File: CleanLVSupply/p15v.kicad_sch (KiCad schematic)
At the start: 19 parts, among them U3 LMR64010XMF, U4 TPS7A47

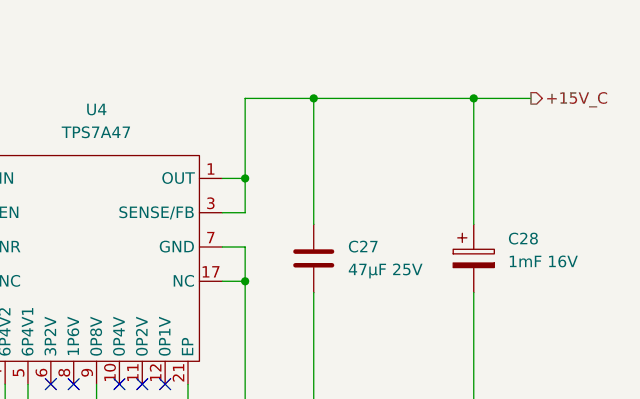
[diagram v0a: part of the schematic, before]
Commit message: HiFiDAC routing done, CleanLVSupply fuses added
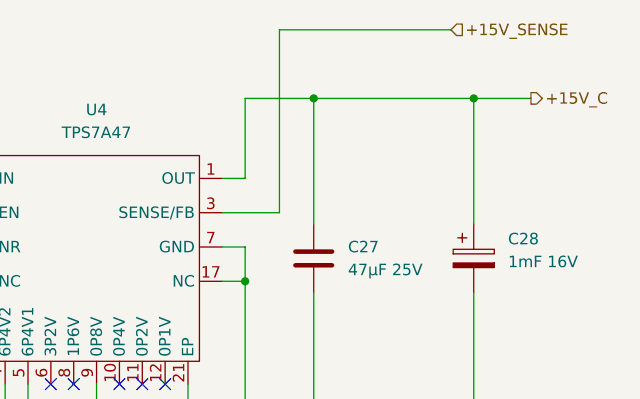
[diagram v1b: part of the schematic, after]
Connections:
- net +15V_C: no longer U4.3 (SENSE/FB)
- new net +15V_SENSE: U4.3 (SENSE/FB)
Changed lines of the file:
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@@
-	)
-	(junction
-		(at 242.57 95.25)
-		(diameter 0)
-		(color 0 0 0 0)
 	)
 	(junction
@@
 	(wire
 		(pts
+			(xy 246.38 99.06) (xy 246.38 78.74)
+		)
+		(stroke
+			(width 0)
+			(type default)
+		)
+	)
+	(wire
+		(pts
 			(xy 152.4 86.36) (xy 168.91 86.36)
 		)
@@
 	(wire
 		(pts
+			(xy 246.38 78.74) (xy 265.43 78.74)
+		)
+		(stroke
+			(width 0)
+			(type default)
+		)
+	)
+	(wire
+		(pts
 			(xy 267.97 86.36) (xy 267.97 100.33)
 		)
@@
 	(wire
 		(pts
-			(xy 242.57 99.06) (xy 242.57 95.25)
-		)
-		(stroke
-			(width 0)
-			(type default)
-		)
-	)
-	(wire
-		(pts
 			(xy 226.06 118.11) (xy 226.06 121.92)
 		)
@@
 	(wire
 		(pts
-			(xy 240.03 99.06) (xy 242.57 99.06)
+			(xy 240.03 99.06) (xy 246.38 99.06)
 		)
 		(stroke
@@
 		)
 	)
+	(hierarchical_label "+15V_SENSE"
+		(shape input)
+		(at 265.43 78.74 0)
+		(fields_autoplaced yes)
+		(effects
+			(font
+				(size 1.27 1.27)
+			)
+			(justify left)
+		)
+	)
